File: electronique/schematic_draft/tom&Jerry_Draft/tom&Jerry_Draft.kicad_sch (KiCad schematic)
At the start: 5 parts, among them IC103 TCA9555RTWR

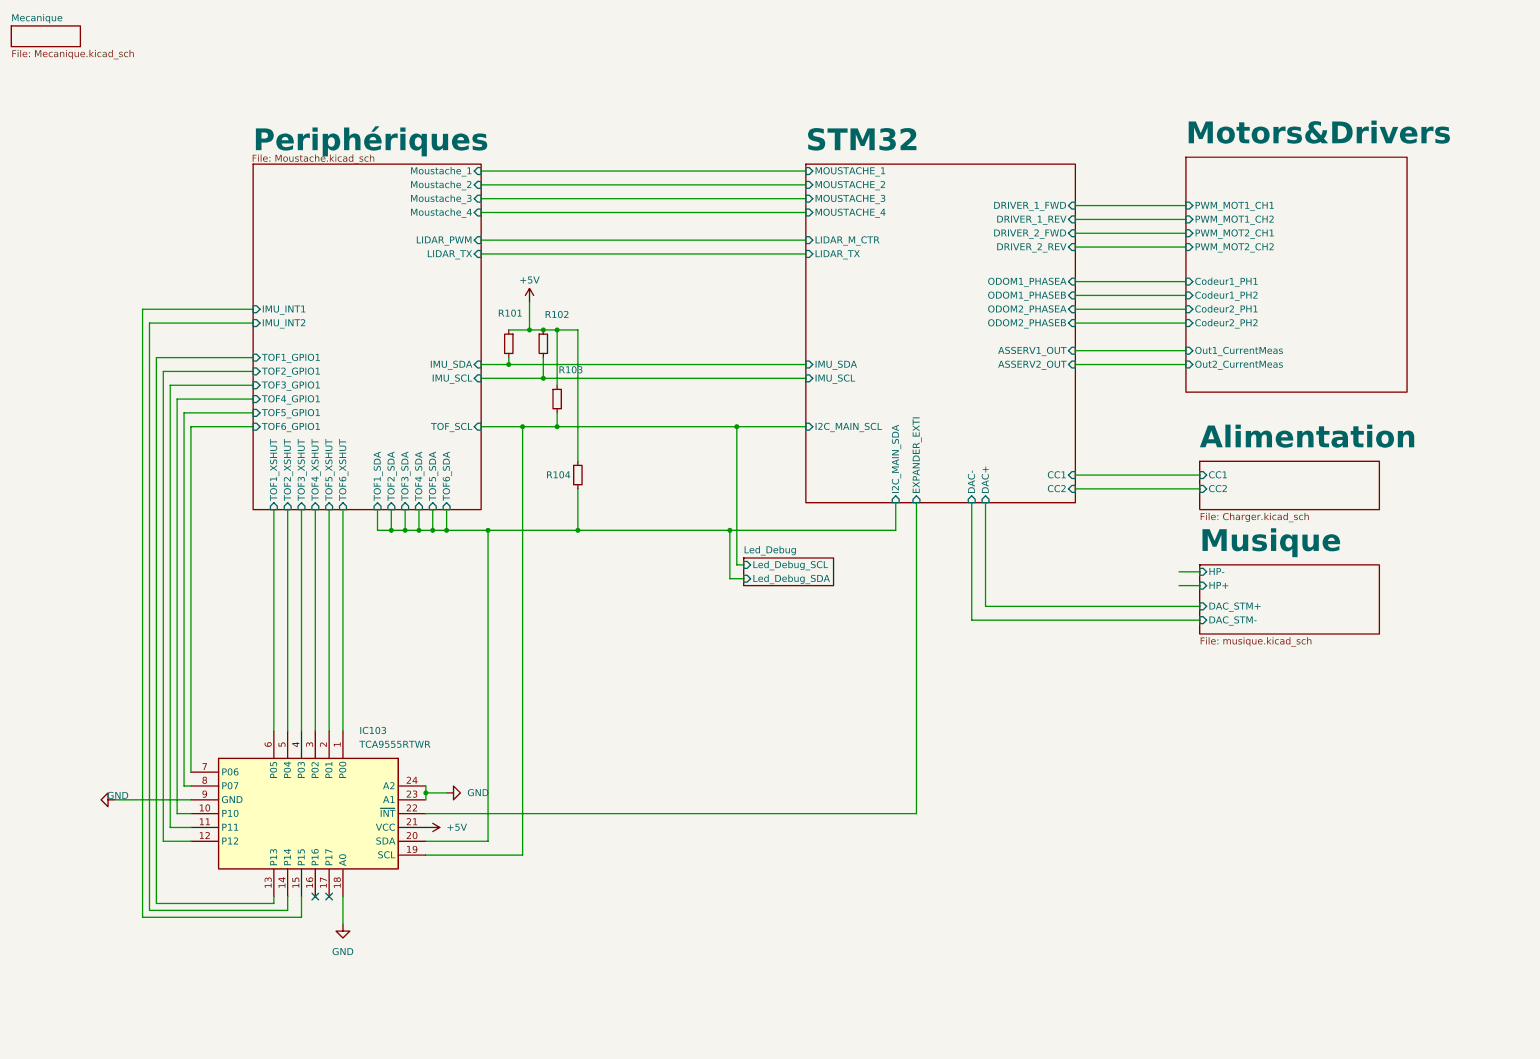
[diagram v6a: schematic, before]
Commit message: STM32 KiCAD v7 x CubeIDE - Correction gpio_expander et driver gpio_expander
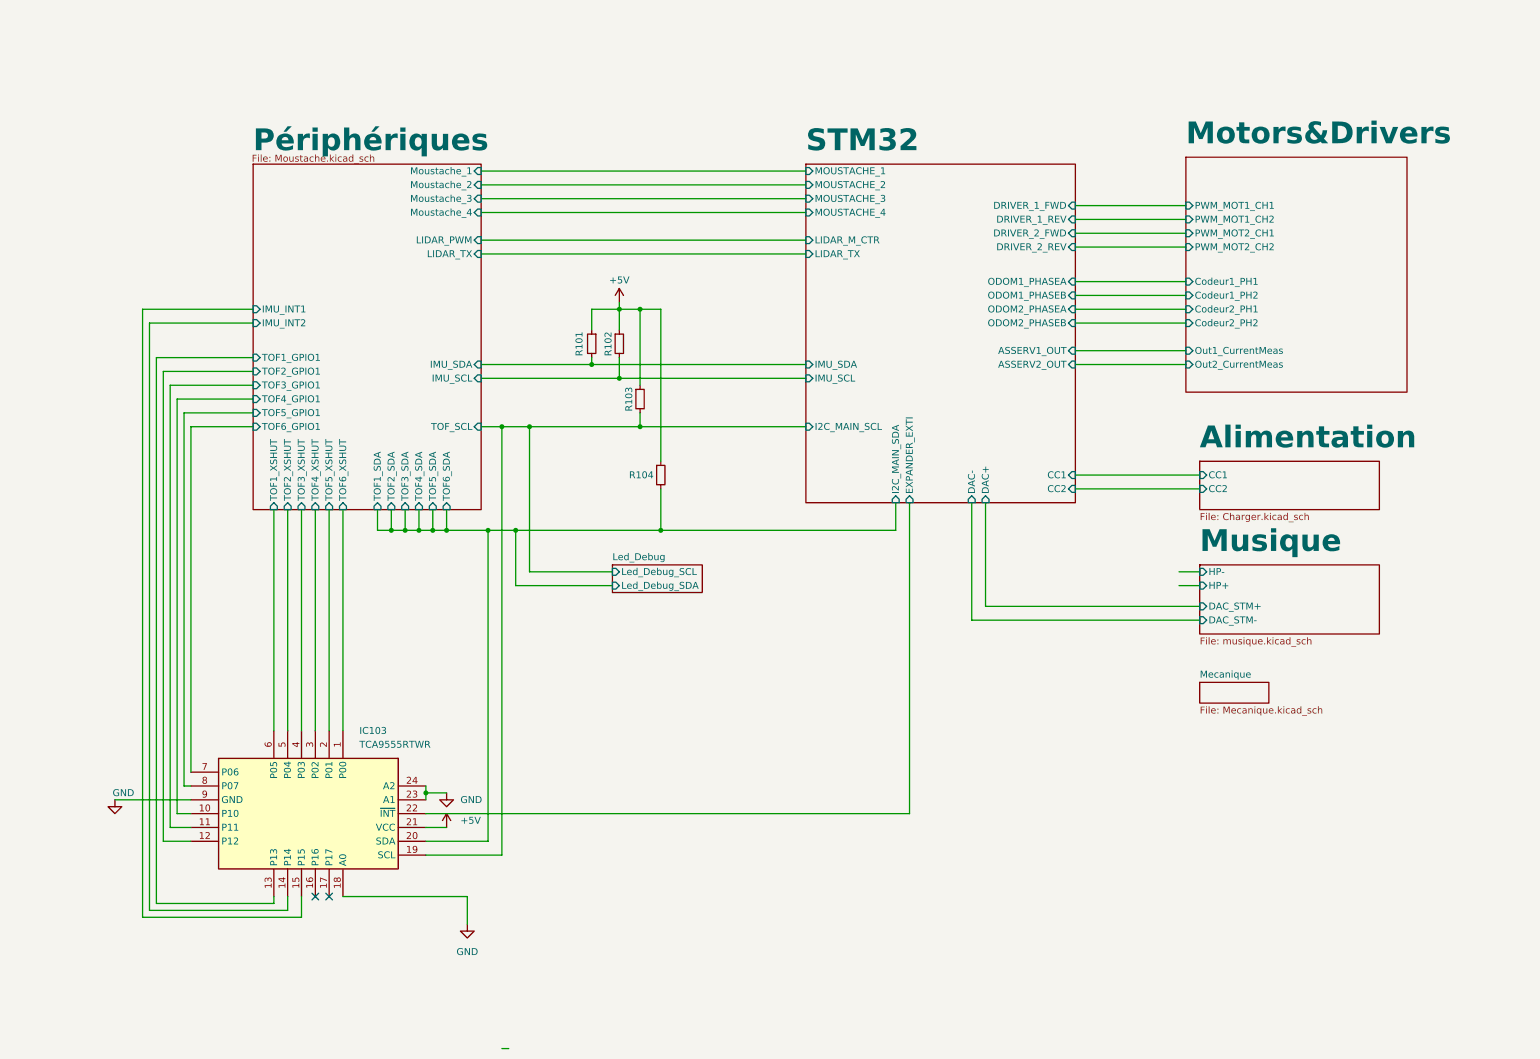
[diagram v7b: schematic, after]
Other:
- sheet Periphériques renamed Périphériques
- moved on the sheet: R101, R102, R103, R104

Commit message: STM32 KiCAD v2.0 x CubeIDE - Pin definitif + schematic reviewed
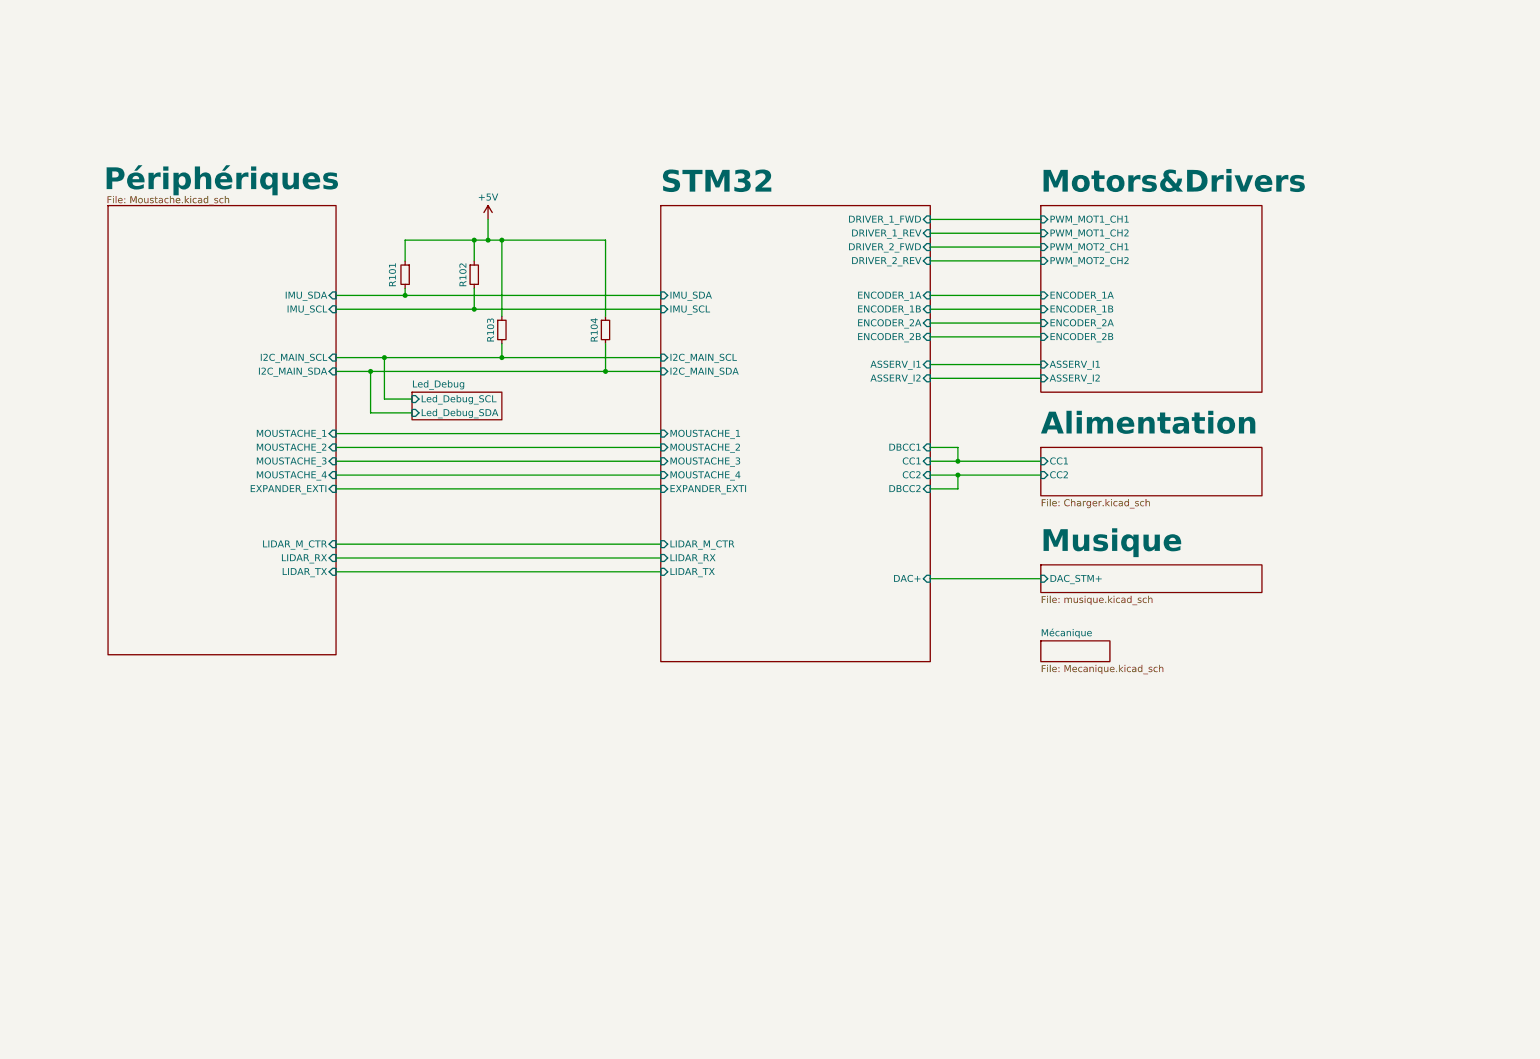
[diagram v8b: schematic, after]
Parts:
- removed IC103: TCA9555RTWR, QFN50P400X400X80-25N-D, symbol TCA9555RTWR:TCA9555RTWR
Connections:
- no-connect marks 2 -> 0
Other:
- sheet Mecanique renamed Mécanique
- sheet Motors&Drivers ports: added ASSERV_I1, ASSERV_I2, ENCODER_1A, ENCODER_1B, ENCODER_2A, ENCODER_2B; removed Codeur1_PH1, Codeur1_PH2, Codeur2_PH1, Codeur2_PH2, Out1_CurrentMeas, Out2_CurrentMeas
- sheet Musique ports: added none; removed DAC_STM-, HP+, HP-
- sheet Périphériques ports: added EXPANDER_EXTI, I2C_MAIN_SCL, I2C_MAIN_SDA, LIDAR_M_CTR, LIDAR_RX, MOUSTACHE_1, MOUSTACHE_2, MOUSTACHE_3, MOUSTACHE_4; removed IMU_INT1, IMU_INT2, LIDAR_PWM, Moustache_1, Moustache_2, Moustache_3, Moustache_4, TOF1_GPIO1, TOF1_SDA, TOF1_XSHUT, TOF2_GPIO1, TOF2_SDA, TOF2_XSHUT, TOF3_GPIO1, TOF3_SDA, TOF3_XSHUT, TOF4_GPIO1, TOF4_SDA, TOF4_XSHUT, TOF5_GPIO1, TOF5_SDA, TOF5_XSHUT, TOF6_GPIO1, TOF6_SDA, TOF6_XSHUT, TOF_SCL
- sheet STM32 ports: added ASSERV_I1, ASSERV_I2, DBCC1, DBCC2, ENCODER_1A, ENCODER_1B, ENCODER_2A, ENCODER_2B, LIDAR_RX; removed ASSERV1_OUT, ASSERV2_OUT, DAC-, ODOM1_PHASEA, ODOM1_PHASEB, ODOM2_PHASEA, ODOM2_PHASEB
- moved on the sheet: R101, R102, R103, R104
